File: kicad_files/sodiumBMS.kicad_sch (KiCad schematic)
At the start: 11 parts, among them J1 USB_C_Receptacle_PowerOnly_6P, U1 STM32F446RETx, U4 LM3940

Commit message: more laying out
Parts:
- C4, C5, C6: footprint (none) -> Capacitor_SMD:C_0805_2012Metric_Pad1.18x1.45mm_HandSolder
- R10, R16, R17, R18, R9: footprint (none) -> Resistor_SMD:R_0805_2012Metric_Pad1.20x1.40mm_HandSolder
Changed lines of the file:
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@@
 			)
 		)
-		(property "Footprint" ""
+		(property "Footprint" "Resistor_SMD:R_0805_2012Metric_Pad1.20x1.40mm_HandSolder"
 			(at 152.4 101.6 0)
 			(hide yes)
@@
 			)
 		)
-		(property "Footprint" ""
+		(property "Footprint" "Resistor_SMD:R_0805_2012Metric_Pad1.20x1.40mm_HandSolder"
 			(at 259.08 88.9 0)
 			(hide yes)
@@
 			)
 		)
-		(property "Footprint" ""
+		(property "Footprint" "Resistor_SMD:R_0805_2012Metric_Pad1.20x1.40mm_HandSolder"
 			(at 259.08 86.36 0)
 			(hide yes)
@@
 			)
 		)
-		(property "Footprint" ""
+		(property "Footprint" "Capacitor_SMD:C_0805_2012Metric_Pad1.18x1.45mm_HandSolder"
 			(at 118.11 52.07 0)
 			(hide yes)
@@
 			)
 		)
-		(property "Footprint" ""
+		(property "Footprint" "Capacitor_SMD:C_0805_2012Metric_Pad1.18x1.45mm_HandSolder"
 			(at 93.98 90.17 0)
 			(hide yes)
@@
 			)
 		)
-		(property "Footprint" ""
+		(property "Footprint" "Resistor_SMD:R_0805_2012Metric_Pad1.20x1.40mm_HandSolder"
 			(at 88.9 85.09 0)
 			(hide yes)
@@
 			)
 		)
-		(property "Footprint" ""
+		(property "Footprint" "Capacitor_SMD:C_0805_2012Metric_Pad1.18x1.45mm_HandSolder"
 			(at 121.92 29.21 0)
 			(hide yes)
@@
 			)
 		)
-		(property "Footprint" ""
+		(property "Footprint" "Resistor_SMD:R_0805_2012Metric_Pad1.20x1.40mm_HandSolder"
 			(at 152.4 109.22 0)
 			(hide yes)

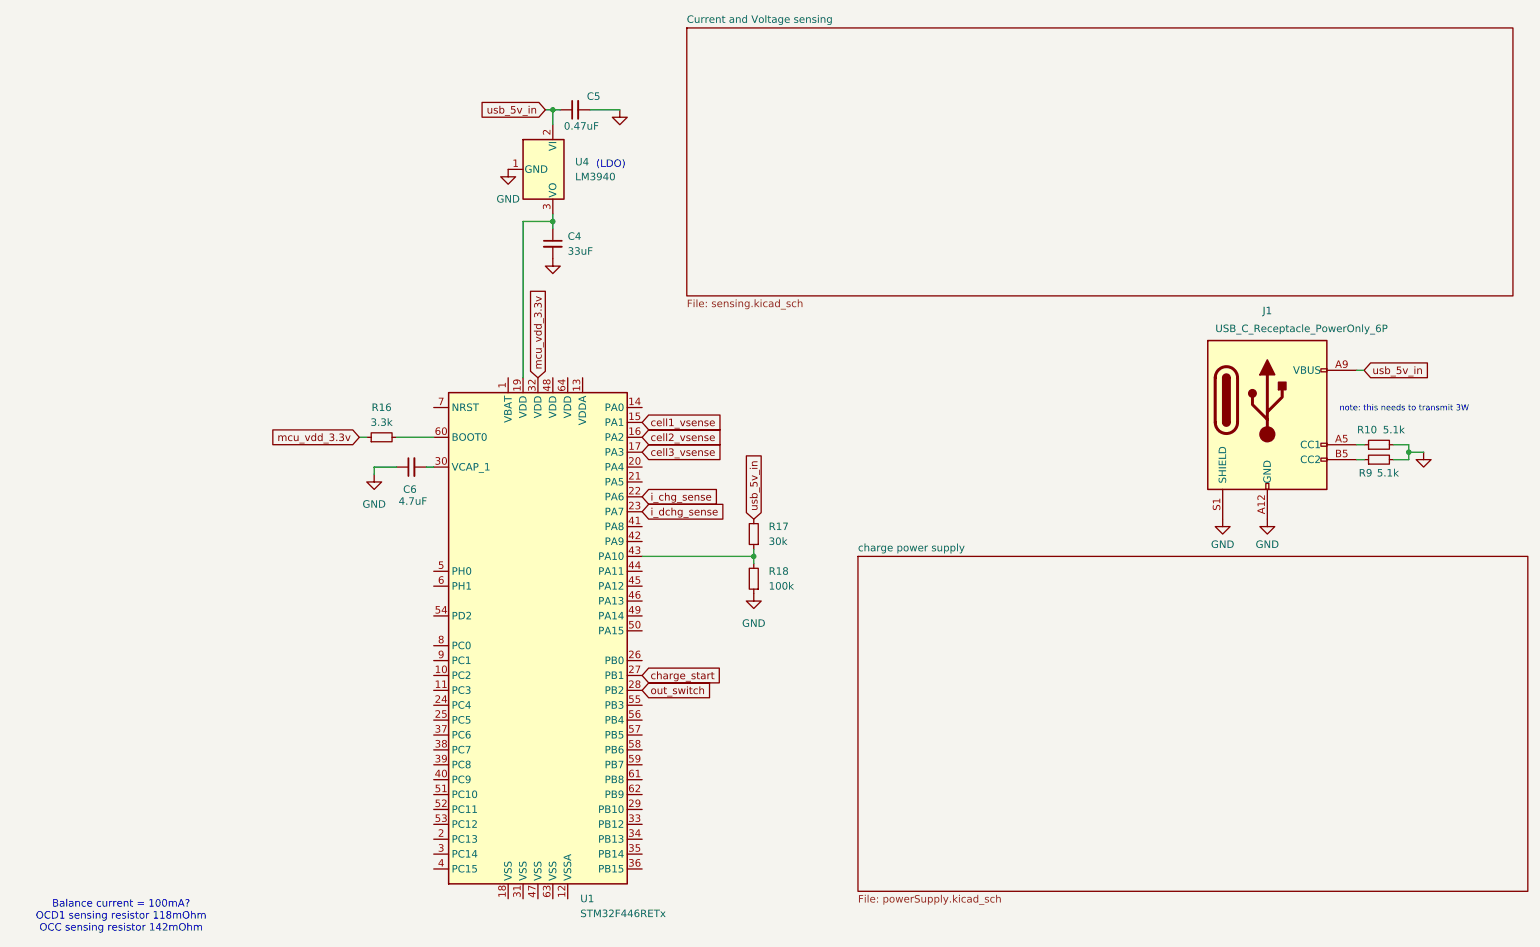
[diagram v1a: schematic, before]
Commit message: Add USB C programming to schematic, with BOOT/RESET buttons
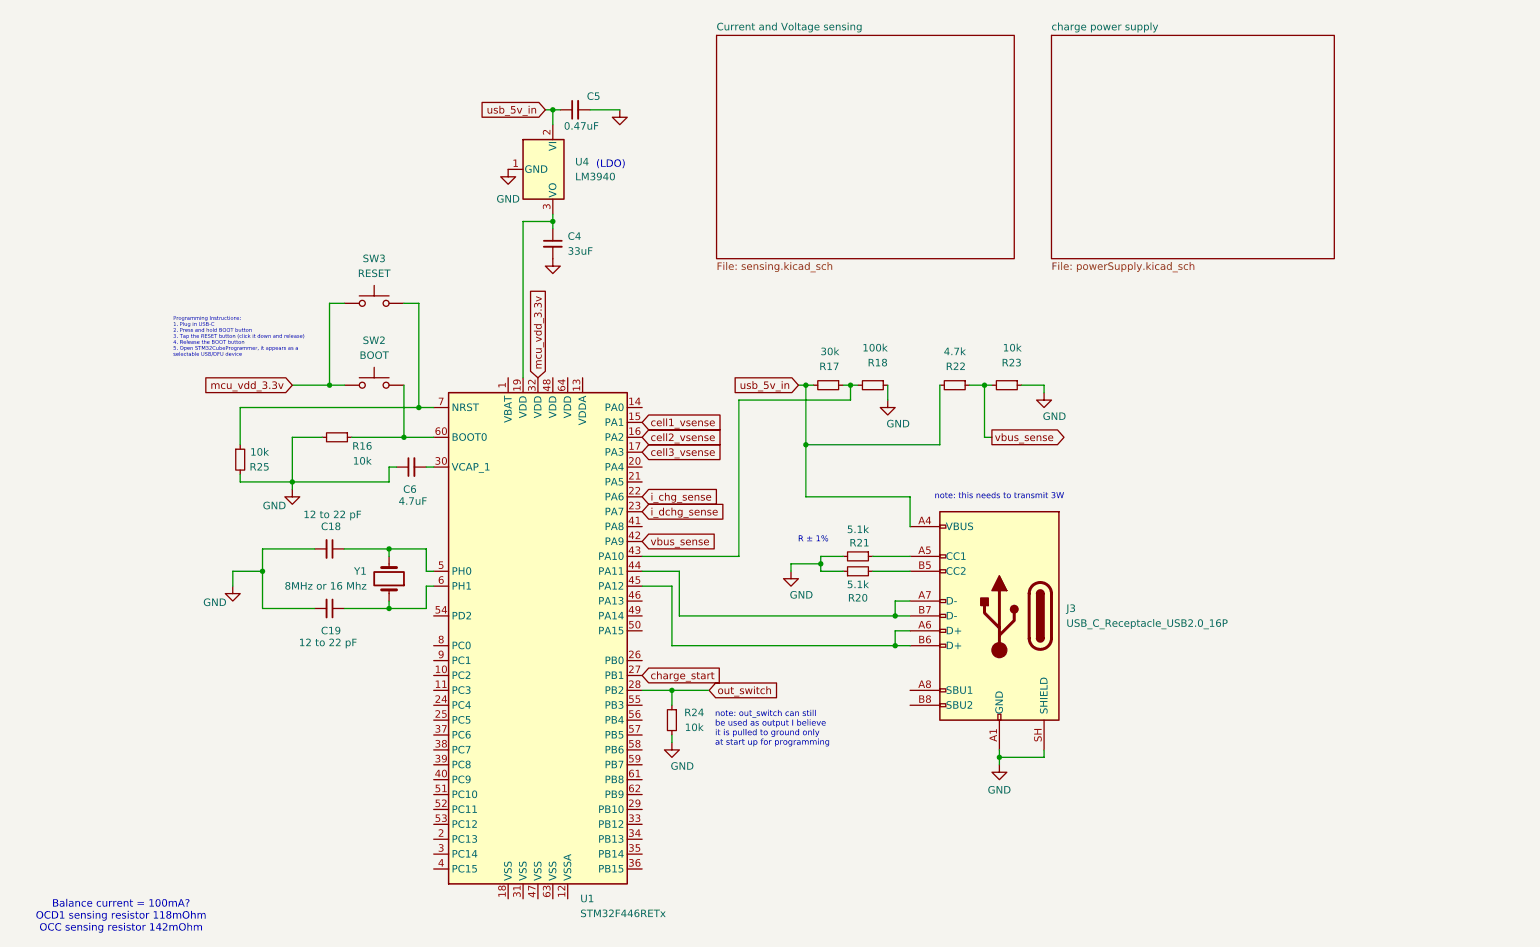
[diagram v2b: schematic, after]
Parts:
- removed J1: USB_C_Receptacle_PowerOnly_6P, symbol Connector:USB_C_Receptacle_PowerOnly_6P
- removed R10, R9: 5.1k, Resistor_SMD:R_0805_2012Metric_Pad1.20x1.40mm_HandSolder, symbol Device:R_Small
- added C18, C19: 12 to 22 pF, Capacitor_SMD:C_0805_2012Metric_Pad1.18x1.45mm_HandSolder, symbol Device:C_Small
- added J3: USB_C_Receptacle_USB2.0_16P, symbol Connector:USB_C_Receptacle_USB2.0_16P
- added R20, R21: 5.1k, Resistor_SMD:R_0805_2012Metric_Pad1.20x1.40mm_HandSolder, symbol Device:R_Small
- added R22: 4.7k, Resistor_SMD:R_0805_2012Metric_Pad1.20x1.40mm_HandSolder, symbol Device:R_Small
- added R23, R24, R25: 10k, Resistor_SMD:R_0805_2012Metric_Pad1.20x1.40mm_HandSolder, symbol Device:R_Small
- added SW2: BOOT, symbol Switch:SW_Push
- added SW3: RESET, symbol Switch:SW_Push
- added Y1: 8MHz or 16 Mhz, symbol Device:Crystal
- R16: value 3.3k -> 10k
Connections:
- net GND: now also R16.2, C18.2, C19.2, J3.A1 (GND), J3.A12 (GND), J3.B1 (GND), J3.B12 (GND), J3.SH (SHIELD), R20.1, R21.2, R23.1, R24.2, R25.2
- net mcu_vdd_3.3v: now also SW2.1, SW3.1; no longer R16.1
- net out_switch: now also R24.1
- net usb_5v_in: now also J3.A4 (VBUS), J3.A9 (VBUS), J3.B4 (VBUS), J3.B9 (VBUS), R22.2
- net vbus_sense: now reaches U1.42 (PA9)
- net vbus_sense: now also R22.1, R23.2
- net at U1.44 (PA11): now also J3.A7 (D-), J3.B7 (D-)
- net at U1.45 (PA12): now also J3.A6 (D+), J3.B6 (D+)
- net at U1.5 (PH0): now also C18.1, Y1.2
- net at U1.6 (PH1): now also C19.1, Y1.1
- net at U1.60 (BOOT0): now also R16.1, SW2.2; no longer R16.2
- net at U1.7 (NRST): now also R25.1, SW3.2
- new net: J3.A5 (CC1), R21.1
- new net: J3.B5 (CC2), R20.2
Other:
- note added: "Programming Instructions: 1. Plug in USB-C 2. Press and hold BOOT button 3. Tap the RESET button (click it down and release) 4. Release the BOOT button 5. Open STM32CubeProgrammer, it appears as a selectable USB/DFU device"
- note added: "R ± 1%"
- note added: "note: out_switch can still be used as output I believe it is pulled to ground only at start up for programming"
- moved on the sheet: R16, R17, R18

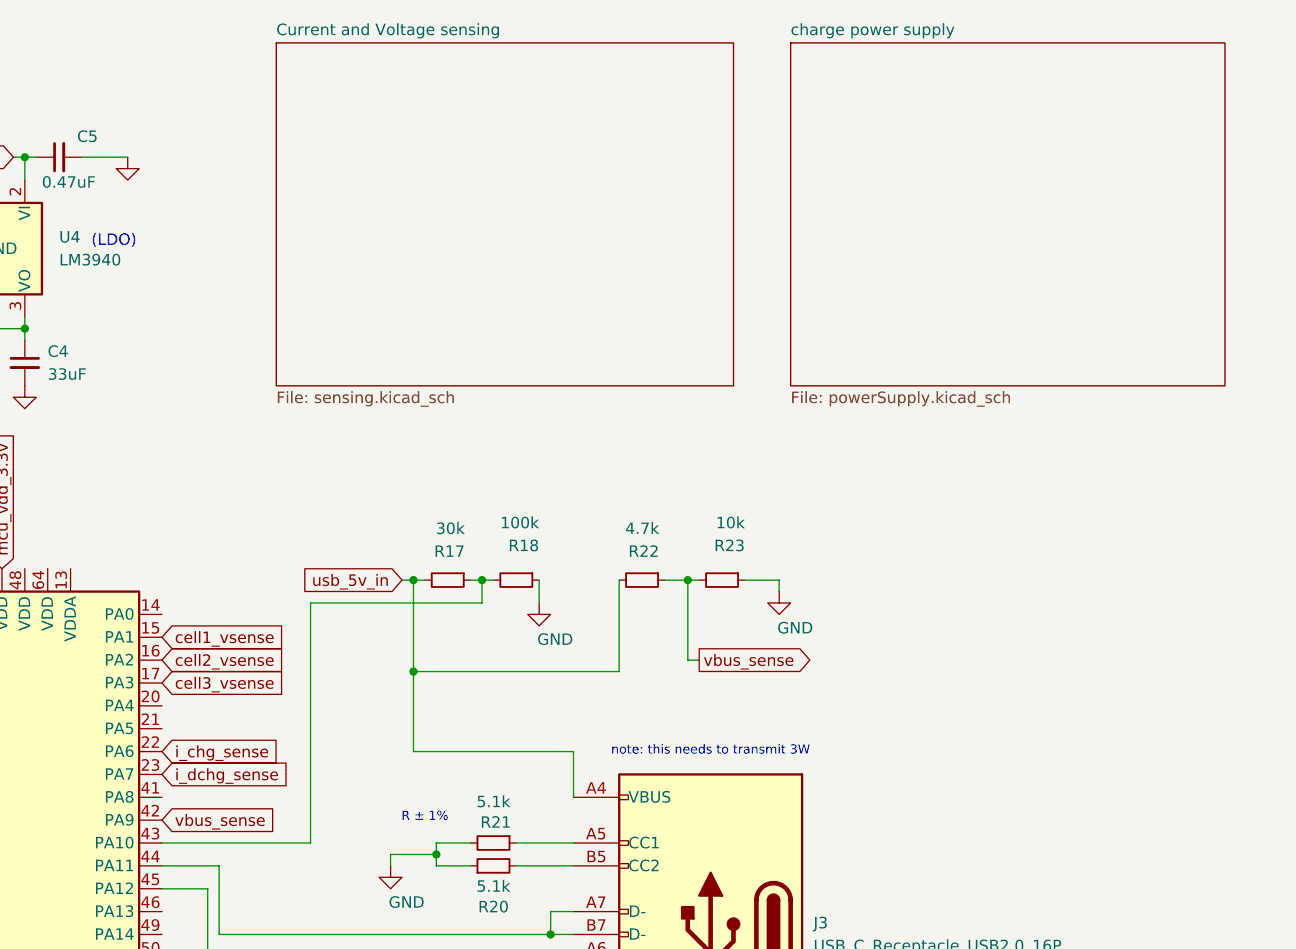
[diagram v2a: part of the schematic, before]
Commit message: Fix sensing schematic and update main schematic
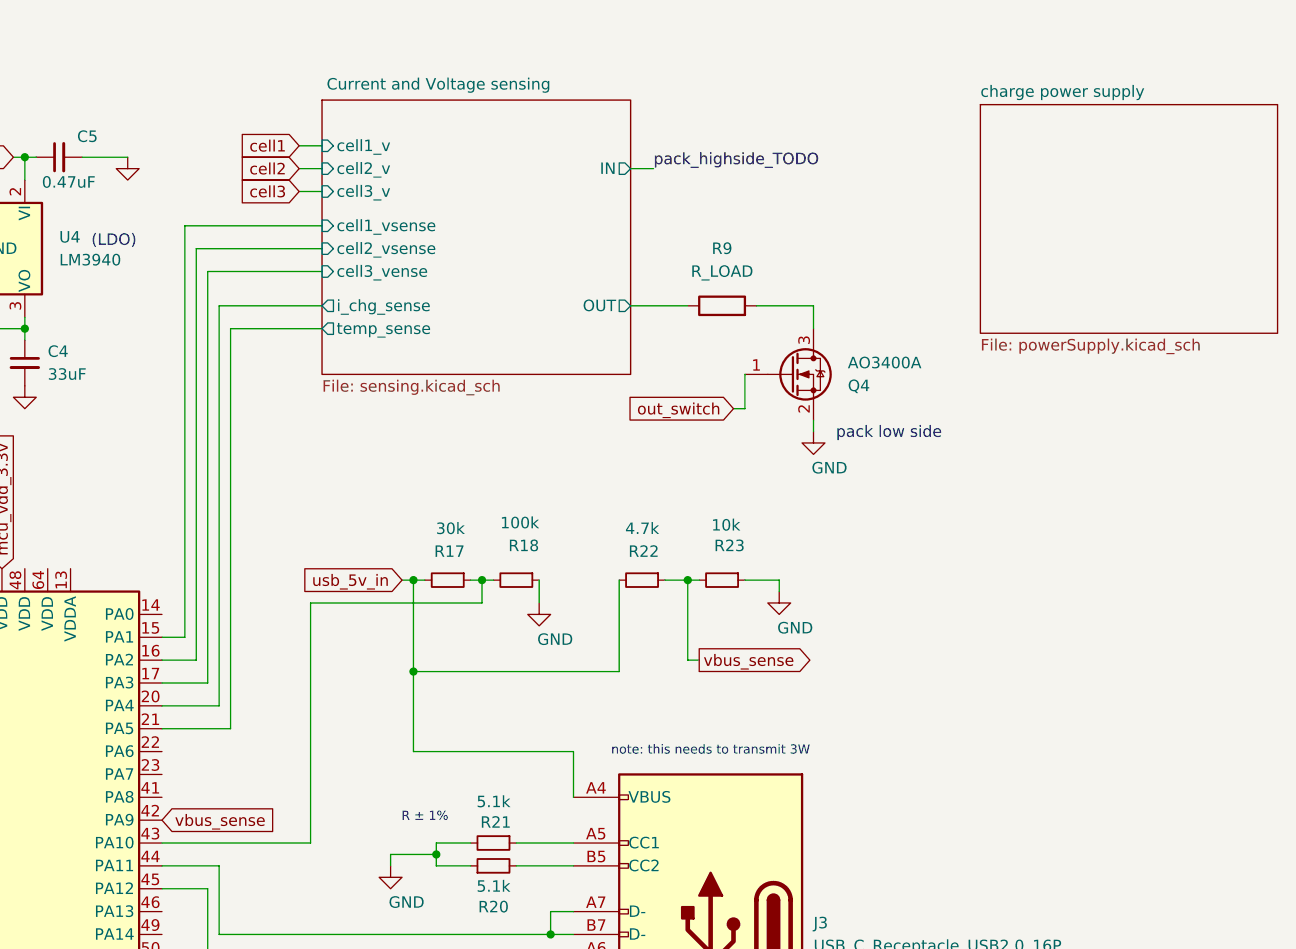
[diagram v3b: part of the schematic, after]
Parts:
- added Q4: AO3400A, Package_TO_SOT_SMD:SOT-23, symbol Transistor_FET:AO3400A
- added R9: R_LOAD, symbol Device:R
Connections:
- net GND: now also Q4.2 (S)
- net out_switch: now also Q4.1 (G)
- net Current and Voltage sensing/i_chg_sense: now reaches U1.20 (PA4)
- net Current and Voltage sensing/temp_sense: now reaches U1.21 (PA5)
- net cell1_vsense renamed Current and Voltage sensing/cell1_vsense
- net cell2_vsense renamed Current and Voltage sensing/cell2_vsense
- net cell3_vsense renamed Current and Voltage sensing/cell3_vense
- net i_chg_sense: no longer names the net of U1.22 (PA6)
- net i_dchg_sense: no longer names the net of U1.23 (PA7)
- new net: Q4.3 (D), R9.2
- new net Current and Voltage sensing/OUT: R9.1
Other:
- sheet Current and Voltage sensing ports: added IN, OUT, cell1_v, cell1_vsense, cell2_v, cell2_vsense, cell3_v, cell3_vense, i_chg_sense, temp_sense; removed none
- note added: "pack low side"

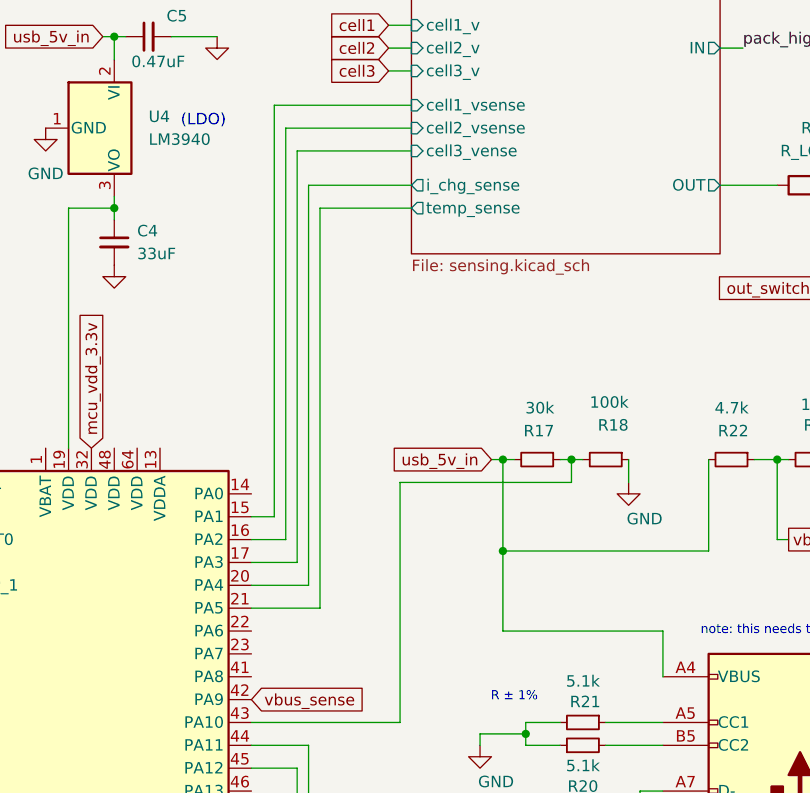
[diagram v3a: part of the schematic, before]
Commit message: Add discharge current measurement
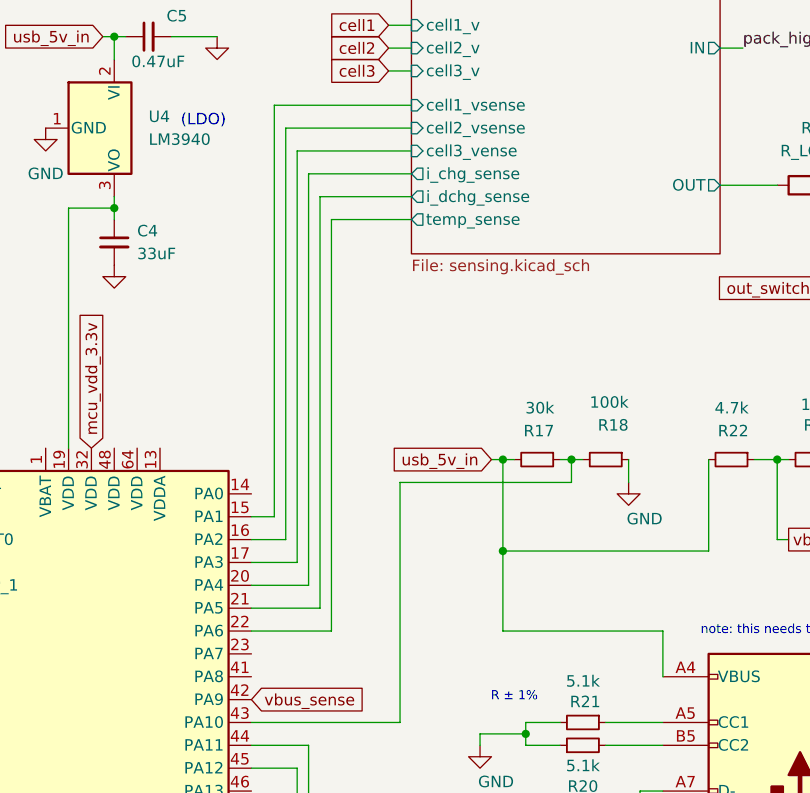
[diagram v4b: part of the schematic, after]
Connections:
- net Current and Voltage sensing/temp_sense: now also U1.22 (PA6); no longer U1.21 (PA5)
- new net Current and Voltage sensing/i_dchg_sense: U1.21 (PA5)
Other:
- sheet Current and Voltage sensing ports: added i_dchg_sense; removed none
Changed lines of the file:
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@@
 	(wire
 		(pts
-			(xy 139.7 45.72) (xy 139.7 90.17)
+			(xy 139.7 44.45) (xy 139.7 90.17)
 		)
 		(stroke
@@
 	(wire
 		(pts
+			(xy 142.24 95.25) (xy 133.35 95.25)
+		)
+		(stroke
+			(width 0)
+			(type default)
+		)
+	)
+	(wire
+		(pts
 			(xy 77.47 104.14) (xy 68.58 104.14)
 		)
@@
 	(wire
 		(pts
+			(xy 151.13 49.53) (xy 142.24 49.53)
+		)
+		(stroke
+			(width 0)
+			(type default)
+		)
+	)
+	(wire
+		(pts
 			(xy 73.66 85.09) (xy 78.74 85.09)
 		)
@@
 	(wire
 		(pts
+			(xy 140.97 46.99) (xy 151.13 46.99)
+		)
+		(stroke
+			(width 0)
+			(type default)
+		)
+	)
+	(wire
+		(pts
 			(xy 163.83 105.41) (xy 163.83 106.68)
 		)
@@
 	(wire
 		(pts
-			(xy 151.13 45.72) (xy 139.7 45.72)
+			(xy 151.13 44.45) (xy 139.7 44.45)
 		)
 		(stroke
@@
 	(wire
 		(pts
-			(xy 151.13 48.26) (xy 140.97 48.26)
-		)
-		(stroke
-			(width 0)
-			(type default)
-		)
-	)
-	(wire
-		(pts
-			(xy 140.97 48.26) (xy 140.97 92.71)
+			(xy 140.97 46.99) (xy 140.97 92.71)
 		)
 		(stroke
@@
 	(wire
 		(pts
+			(xy 142.24 49.53) (xy 142.24 95.25)
+		)
+		(stroke
+			(width 0)
+			(type default)
+		)
+	)
+	(wire
+		(pts
 			(xy 96.52 104.14) (xy 96.52 107.95)
 		)
@@
 		)
 		(pin "i_chg_sense" output
-			(at 151.13 45.72 180)
+			(at 151.13 44.45 180)
 			(effects
 				(font
@@
 		)
 		(pin "temp_sense" output
-			(at 151.13 48.26 180)
+			(at 151.13 49.53 180)
+			(effects
+				(font
+					(size 1.27 1.27)
+				)
+				(justify left)
+			)
+		)
+		(pin "i_dchg_sense" output
+			(at 151.13 46.99 180)
 			(effects
 				(font
